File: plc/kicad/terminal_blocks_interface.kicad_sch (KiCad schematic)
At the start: 80 parts, among them CN1 DB128V-5.08-2P-GN-S, CN10 DB128V-5.08-2P-GN-S, CN13 DB128V-5.08-2P-GN-S, CN14 DB128V-5.08-2P-GN-S, CN2 DB128V-5.08-2P-GN-S, CN3 DB128V-5.08-2P-GN-S, CN4 DB128V-5.08-2P-GN-S, CN5 DB128V-5.08-2P-GN-S, CN6 DB128V-5.08-2P-GN-S, CN7 DB128V-5.08-2P-GN-S, CN8 DB128V-5.08-2P-GN-S, CN9 DB128V-5.08-2P-GN-S, Q1 AO3400A, Q2 AO3400A, U1 TCA9535PWR, U2 TPS272C45DRHFR, U3 TPS272C45DRHFR, U4 ADS1115IDGSR, U5 LTV-814S-TA1-A, U6 LTV-814S-TA1-A, U7 LTV-814S-TA1-A, U8 LTV-814S-TA1-A

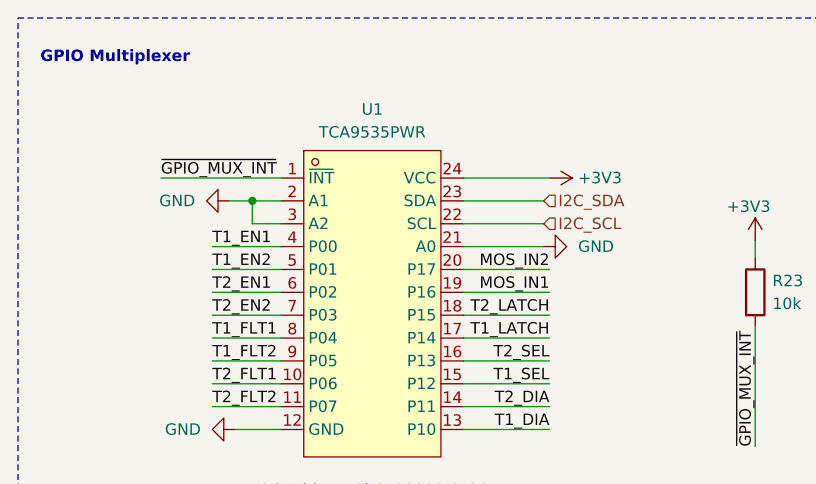
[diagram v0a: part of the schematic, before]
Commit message: Add schematic digital output expansion
Co-authored-by: arena-agent <297053741+arena-agent@users.noreply.github.com>
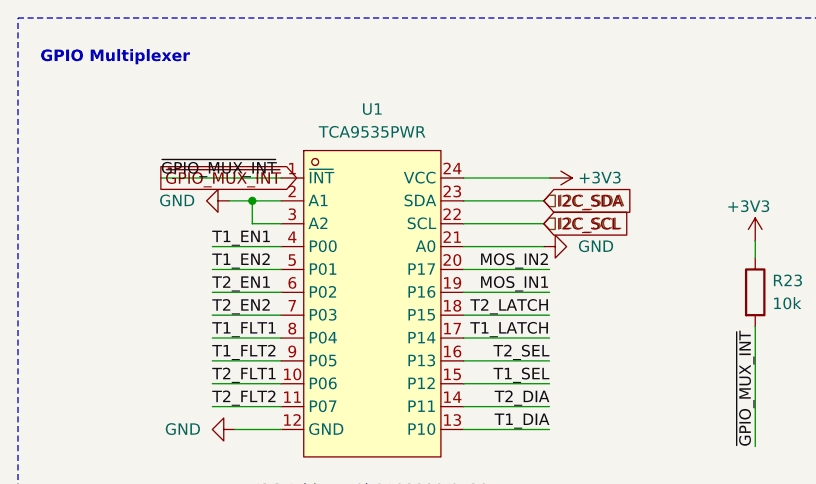
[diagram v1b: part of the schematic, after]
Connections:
- net ~{MUX_INT} renamed ~{GPIO_MUX_INT}
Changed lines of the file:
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@@
 		)
+	)
+	(global_label "I2C_SDA"
+		(shape input)
+		(at 77.47 37.465 0)
+		(effects (font (size 1.27 1.27)) (justify left bottom))
+	)
+	(global_label "I2C_SCL"
+		(shape input)
+		(at 77.47 40.005 0)
+		(effects (font (size 1.27 1.27)) (justify left bottom))
+	)
+	(global_label "~{GPIO_MUX_INT}"
+		(shape output)
+		(at 34.925 34.925 0)
+		(effects (font (size 1.27 1.27)) (justify left bottom))
 	)
 	(symbol
